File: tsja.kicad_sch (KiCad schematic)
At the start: 66 parts, among them J1 QWIIC, J2 Micro_SD_Card, J3 SAO, J4 EXT, J6 USB-C, M1 Vibration, Q1 AP2302B, Q4 AO3400 (A09T), Q5 AO3400 (A09T), T1 Select, T2 Start, T3 B, T4 A, T5 Cross, U1 74LVC1G17GW,125, U10 SY6280AAC, U11 SK6805, U12 SK6805, U13 SK6805, U14 SK6805, U15 SK6805, U2 MPR121QR2, U3 ESP32-WROVER-E, U7 CH340K, U8 SK6805, U9 SY6280AAC

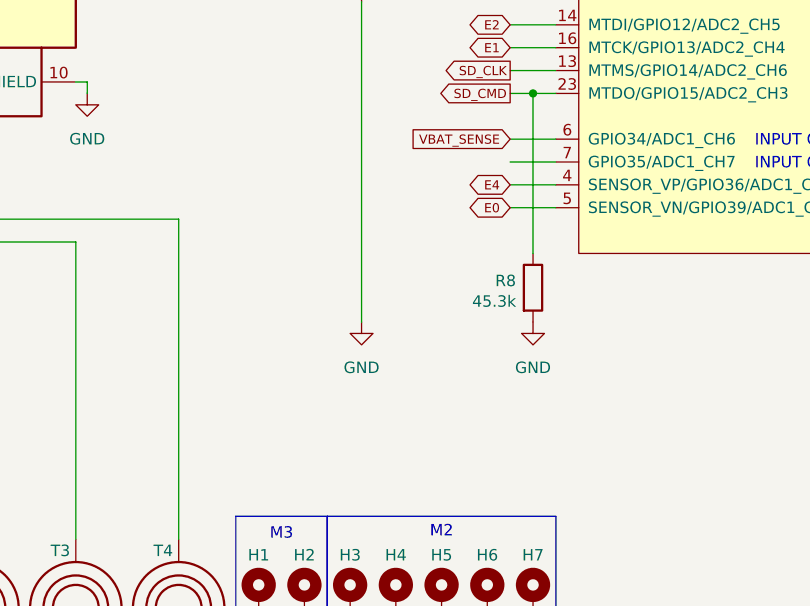
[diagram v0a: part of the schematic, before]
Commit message: Use DC/DC from WHY badge
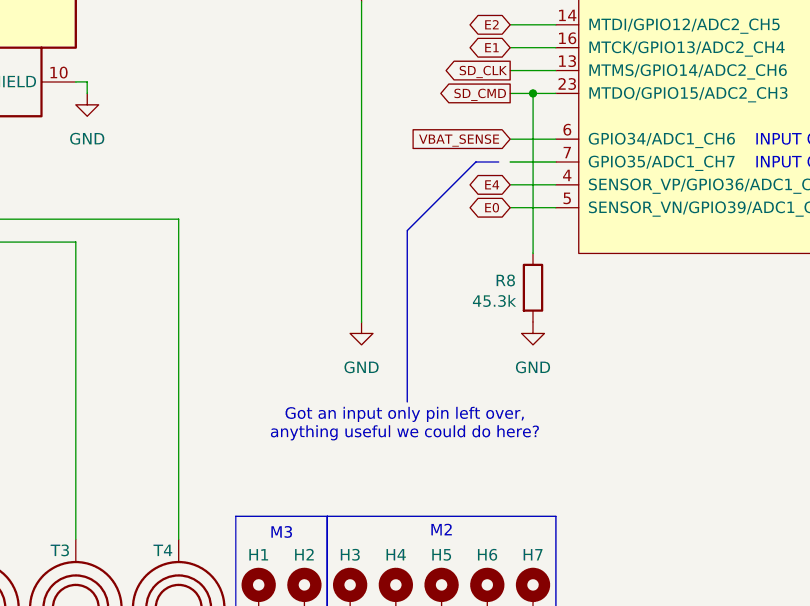
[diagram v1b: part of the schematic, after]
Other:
- note added: "Got an input only pin left over, anything useful we could do here?"
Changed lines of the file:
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@@
 	(title_block
 		(title "TSJA badge")
-		(date "2024-12-04")
+		(date "2024-12-06")
 		(rev "1.0")
 		(company "Nicolai Electronics")
@@
 		)
 	)
+	(polyline
+		(pts
+			(xy 160.02 166.37) (xy 160.02 147.32)
+		)
+		(stroke
+			(width 0)
+			(type default)
+		)
+	)
 	(wire
 		(pts
@@
 		)
 	)
+	(polyline
+		(pts
+			(xy 160.02 147.32) (xy 167.64 139.7)
+		)
+		(stroke
+			(width 0)
+			(type default)
+		)
+	)
 	(wire
 		(pts
@@
 		(pts
 			(xy 223.52 77.47) (xy 223.52 85.09)
+		)
+		(stroke
+			(width 0)
+			(type default)
+		)
+	)
+	(polyline
+		(pts
+			(xy 167.64 139.7) (xy 170.18 139.7)
 		)
 		(stroke
@@
 		)
 	)
+	(text "Got an input only pin left over,\nanything useful we could do here?"
+		(exclude_from_sim no)
+		(at 159.766 168.91 0)
+		(effects
+			(font
+				(size 1.27 1.27)
+			)
+		)
+	)

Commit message: Small fixes
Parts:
- H2: footprint MountingHole:MountingHole_3.2mm_M3_DIN965_Pad_TopOnly -> MountingHole:MountingHole_3.2mm_M3_DIN965; symbol Mechanical:MountingHole_Pad -> Mechanical:MountingHole
- H5: footprint MountingHole:MountingHole_2.7mm_M2.5_Pad_TopOnly -> MountingHole:MountingHole_2.7mm_M2.5_DIN965; symbol Mechanical:MountingHole_Pad -> Mechanical:MountingHole
- U2: LCSC (none) -> C91322
- U9: Buy early Y -> (none); Category ICs -> (none); MPN SY6280AAC -> (none); Manufacturer Silergy Corp -> (none); Mouser - -> (none); Sponsored N -> (none)
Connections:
- net GND: no longer H2.1, H5.1
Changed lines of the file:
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@@
 			)
 		)
-		(property "Mouser" "-"
-			(at 106.68 82.55 0)
-			(effects
-				(font
-					(size 1.27 1.27)
-				)
-				(hide yes)
-			)
-		)
-		(property "Price" ""
-			(at 106.68 82.55 0)
-			(effects
-				(font
-					(size 1.27 1.27)
-				)
-				(hide yes)
-			)
-		)
-		(property "Sponsored" "N"
-			(at 106.68 82.55 0)
-			(effects
-				(font
-					(size 1.27 1.27)
-				)
-				(hide yes)
-			)
-		)
-		(property "Category" "ICs"
-			(at 106.68 82.55 0)
-			(effects
-				(font
-					(size 1.27 1.27)
-				)
-				(hide yes)
-			)
-		)
-		(property "Buy early" "Y"
-			(at 106.68 82.55 0)
-			(effects
-				(font
-					(size 1.27 1.27)
-				)
-				(hide yes)
-			)
-		)
-		(property "MPN" "SY6280AAC"
-			(at 106.68 82.55 0)
-			(effects
-				(font
-					(size 1.27 1.27)
-				)
-				(hide yes)
-			)
-		)
-		(property "Manufacturer" "Silergy Corp"
-			(at 106.68 82.55 0)
-			(effects
-				(font
-					(size 1.27 1.27)
-				)
-				(hide yes)
-			)
-		)
 		(pin "1"
 		)
@@
 	)
 	(symbol
-		(lib_id "power:GND")
-		(at 148.59 190.5 0)
-		(unit 1)
-		(exclude_from_sim no)
-		(in_bom yes)
-		(on_board yes)
-		(dnp no)
-		(fields_autoplaced yes)
-		(property "Reference" "#PWR02"
-			(at 148.59 196.85 0)
-			(effects
-				(font
-					(size 1.27 1.27)
-				)
-				(hide yes)
-			)
-		)
-		(property "Value" "GND"
-			(at 148.59 195.58 0)
-			(effects
-				(font
-					(size 1.27 1.27)
-				)
-			)
-		)
-		(property "Footprint" ""
-			(at 148.59 190.5 0)
-			(effects
-				(font
-					(size 1.27 1.27)
-				)
-				(hide yes)
-			)
-		)
-		(property "Datasheet" ""
-			(at 148.59 190.5 0)
-			(effects
-				(font
-					(size 1.27 1.27)
-				)
-				(hide yes)
-			)
-		)
-		(property "Description" "Power symbol creates a global label with name \"GND\" , ground"
-			(at 148.59 190.5 0)
-			(effects
-				(font
-					(size 1.27 1.27)
-				)
-				(hide yes)
-			)
-		)
-		(pin "1"
-		)
-		(instances
-			(project "tsja"
-				(path "/5f312b85-6822-40a3-b417-2df49696ca2d"
-					(reference "#PWR02")
-					(unit 1)
-				)
-			)
-		)
-	)
-	(symbol
 		(lib_id "mch2021-rescue:C-Device")
 		(at 144.78 34.29 0)
@@
 	)
 	(symbol
-		(lib_id "power:GND")
-		(at 163.83 190.5 0)
-		(unit 1)
-		(exclude_from_sim no)
-		(in_bom yes)
-		(on_board yes)
-		(dnp no)
-		(fields_autoplaced yes)
-		(property "Reference" "#PWR020"
-			(at 163.83 196.85 0)
-			(effects
-				(font
-					(size 1.27 1.27)
-				)
-				(hide yes)
-			)
-		)
-		(property "Value" "GND"
-			(at 163.83 195.58 0)
-			(effects
-				(font
-					(size 1.27 1.27)
-				)
-			)
-		)
-		(property "Footprint" ""
-			(at 163.83 190.5 0)
-			(effects
-				(font
-					(size 1.27 1.27)
-				)
-				(hide yes)
-			)
-		)
-		(property "Datasheet" ""
-			(at 163.83 190.5 0)
-			(effects
-				(font
-					(size 1.27 1.27)
-				)
-				(hide yes)
-			)
-		)
-		(property "Description" "Power symbol creates a global label with name \"GND\" , ground"
-			(at 163.83 190.5 0)
-			(effects
-				(font
-					(size 1.27 1.27)
-				)
-				(hide yes)
-			)
-		)
-		(pin "1"
-		)
-		(instances
-			(project "tsja"
-				(path "/5f312b85-6822-40a3-b417-2df49696ca2d"
-					(reference "#PWR020")
-					(unit 1)
-				)
-			)
-		)
-	)
-	(symbol
 		(lib_id "Sensor_Touch:MPR121QR2")
 		(at 45.72 161.29 0)
@@
 			)
 		)
+		(property "LCSC" "C91322"
+			(at 45.72 161.29 0)
+			(effects
+				(font
+					(size 1.27 1.27)
+				)
+				(hide yes)
+			)
+		)
 		(pin "16"
 		)
@@
 	)
 	(symbol
-		(lib_id "Mechanical:MountingHole_Pad")
-		(at 163.83 187.96 0)
+		(lib_id "Mechanical:MountingHole")
+		(at 163.83 186.69 0)
 		(unit 1)
 		(exclude_from_sim yes)
@@
 		)
 		(property "Value" "~"
-			(at 166.37 187.9599 0)
+			(at 166.37 186.6899 0)
 			(effects
 				(font
@@
 			)
 		)
-		(property "Footprint" "MountingHole:MountingHole_2.7mm_M2.5_Pad_TopOnly"
-			(at 163.83 187.96 0)
+		(property "Footprint" "MountingHole:MountingHole_2.7mm_M2.5_DIN965"
+			(at 163.83 186.69 0)
 			(effects
 				(font
@@
 		)
 		(property "Datasheet" "~"
-			(at 163.83 187.96 0)
+			(at 163.83 186.69 0)
 			(effects
 				(font
@@
 			)
 		)
-		(property "Description" "Mounting Hole with connection"
-			(at 163.83 187.96 0)
+		(property "Description" "Mounting Hole without connection"
+			(at 163.83 186.69 0)
 			(effects
 				(font
@@
 			)
 		)
-		(pin "1"
-		)
 		(instances
 			(project "tsja"
@@
 	)
 	(symbol
-		(lib_id "Mechanical:MountingHole_Pad")
-		(at 148.59 187.96 0)
+		(lib_id "Mechanical:MountingHole")
+		(at 148.59 186.69 0)
 		(unit 1)
 		(exclude_from_sim yes)
@@
 		)
 		(property "Value" "~"
-			(at 151.13 187.9599 0)
+			(at 151.13 186.6899 0)
 			(effects
 				(font
@@
 			)
 		)
-		(property "Footprint" "MountingHole:MountingHole_3.2mm_M3_DIN965_Pad_TopOnly"
-			(at 148.59 187.96 0)
+		(property "Footprint" "MountingHole:MountingHole_3.2mm_M3_DIN965"
+			(at 148.59 186.69 0)
 			(effects
 				(font
@@
 		)
 		(property "Datasheet" "~"
-			(at 148.59 187.96 0)
+			(at 148.59 186.69 0)
 			(effects
 				(font
@@
 			)
 		)
-		(property "Description" "Mounting Hole with connection"
-			(at 148.59 187.96 0)
+		(property "Description" "Mounting Hole without connection"
+			(at 148.59 186.69 0)
 			(effects
 				(font
@@
 			)
 		)
-		(pin "1"
-		)
 		(instances

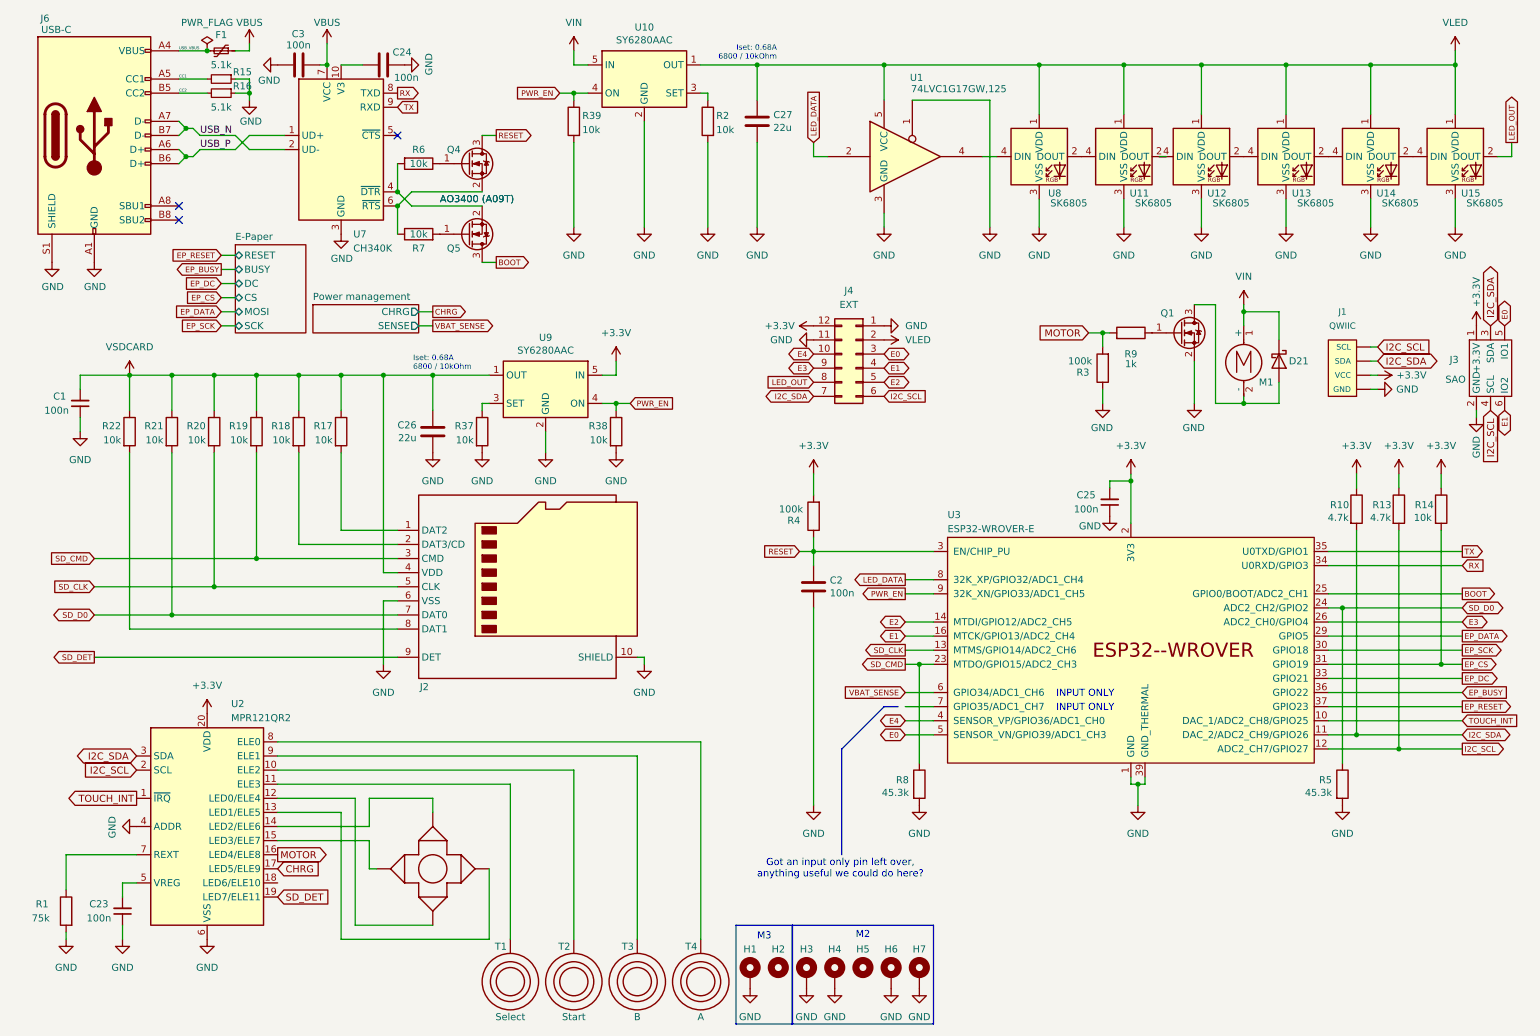
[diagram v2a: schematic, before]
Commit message: No DRC errors
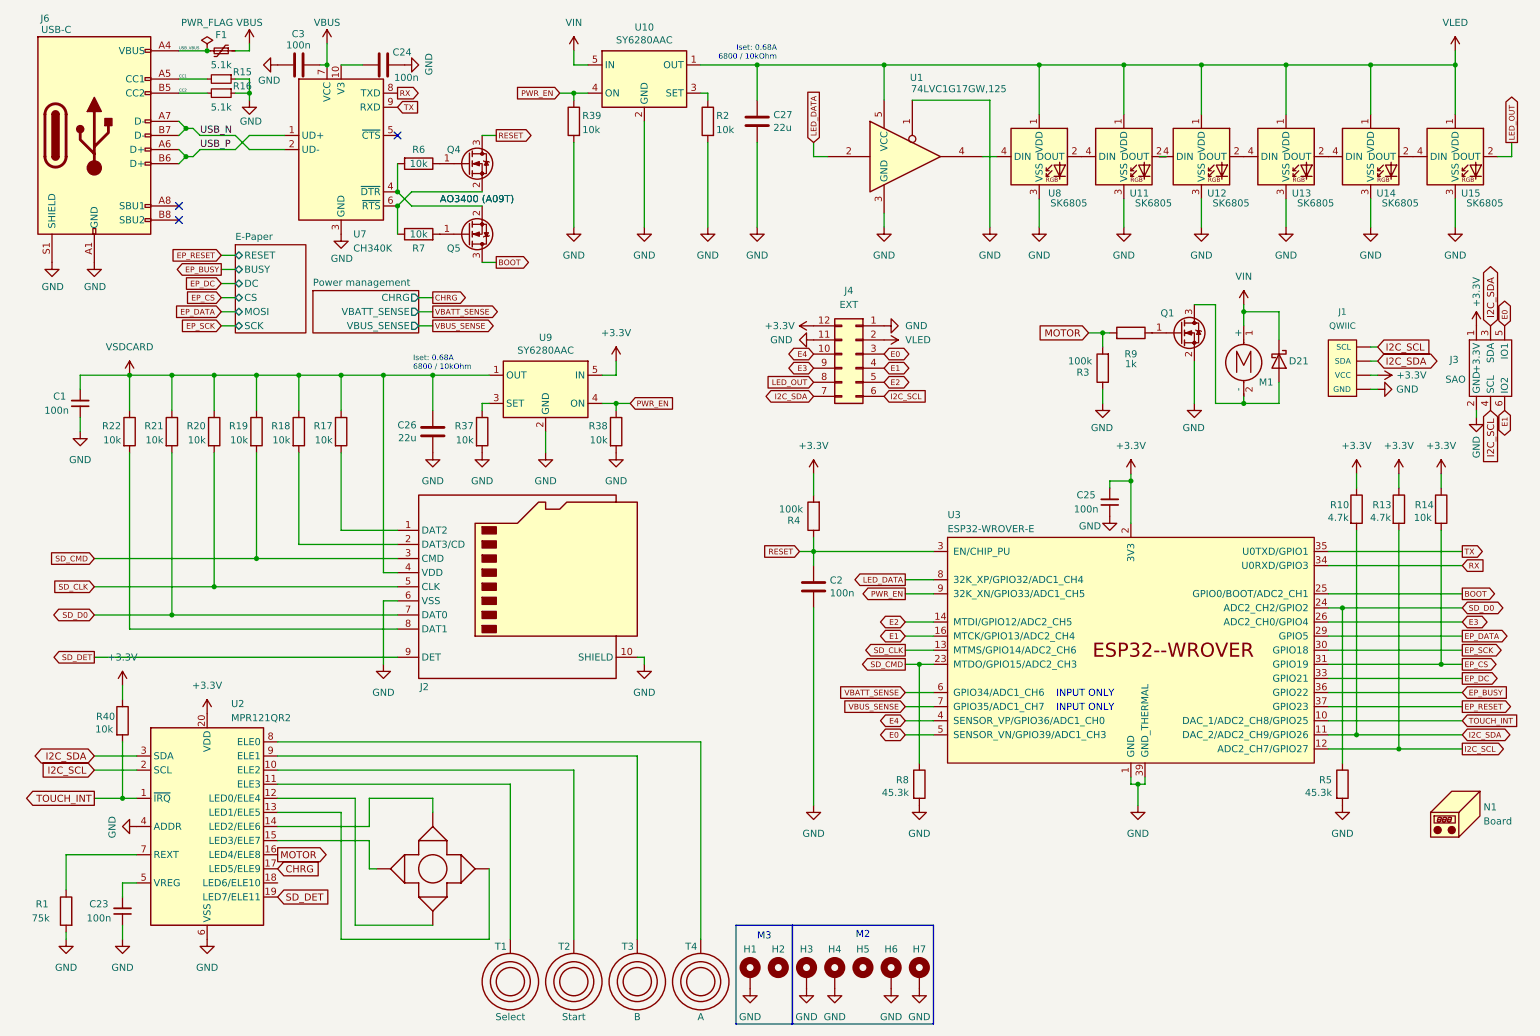
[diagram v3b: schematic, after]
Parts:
- added N1: Board, design:board, symbol Mechanical:Housing
- added R40: 10k, Resistor_SMD:R_0402_1005Metric, symbol mch2021-rescue:R-Device
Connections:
- net +3.3V: now also R40.1
- net TOUCH_INT: now also R40.2
- net VBUS_SENSE: now reaches U3.7 (GPIO35/ADC1_CH7)
- net VBAT_SENSE renamed VBATT_SENSE
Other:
- sheet Power management ports: added VBATT_SENSE, VBUS_SENSE; removed SENSE
- note removed: "Got an input only pin left over, anything useful we could do here?"

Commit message: Cleanup & tweaks
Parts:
- C2, C24, C3: LCSC C307331 -> (none)
- C26, C27: Buy early Y -> (none); Category Capacitors -> (none); LCSC C602037 -> (none); MPN CL21A226MAYNNNE -> (none); Manufacturer Samsung Electro-Mechanics -> (none); Minimal voltage rating 10 -> (none); Sponsored N -> (none); Voltage rating 25 -> (none)
- M1: footprint Connector_PinHeader_2.00mm:PinHeader_1x02_P2.00mm_Vertical -> Connector_PinHeader_2.54mm:PinHeader_1x02_P2.54mm_Vertical_SMD_Pin1Left
- R6, R7: LCSC C60490 -> (none)
- U10: Buy early Y -> (none); Category ICs -> (none); MPN SY6280AAC -> (none); Manufacturer Silergy Corp -> (none); Mouser - -> (none); Sponsored N -> (none)

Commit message: Apply fixes proposed by Paul
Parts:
- added C31: 22u, Capacitor_SMD:C_0805_2012Metric, symbol Device:C
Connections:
- net VIN: now also C31.1
- net at D21.2 (A), M1.2 (-), Q1.3 (D): now also C31.2
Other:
- moved on the sheet: D21, M1, Q1, R3, R40, R9

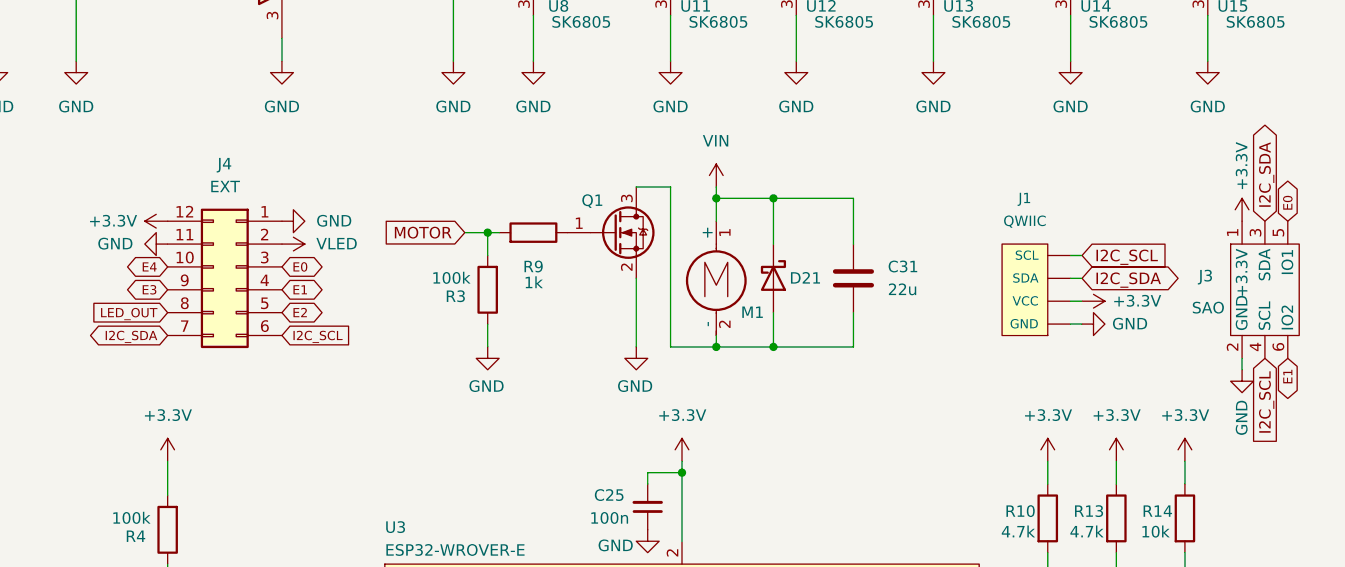
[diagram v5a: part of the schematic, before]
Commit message: Fill out BOM, add labels to PCB
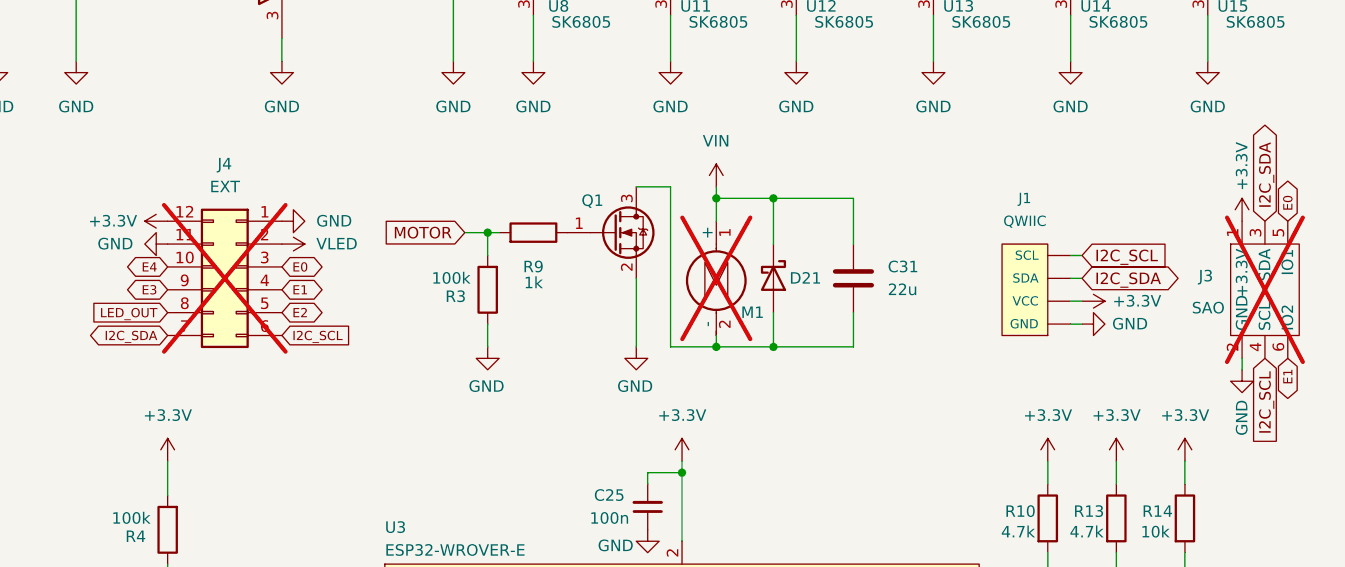
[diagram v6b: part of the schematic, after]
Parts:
- C1, C2, C23, C24, C25, C3: LCSC (none) -> C307331
- C26, C27, C31: LCSC (none) -> C45783
- H1, H2, H3, H4, H5, H6, H7: LCSC (none) -> -
- J3, J4: now not fitted; now left out of the parts list
- M1: LCSC (none) -> -; now not fitted; now left out of the parts list
- N1, T1, T2, T3, T4, T5: LCSC (none) -> -; now left out of the parts list
- R1: LCSC (none) -> C25798
- R10, R13: LCSC (none) -> C25940
- R14, R17, R18, R19, R2, R20, R21, R22, R37, R38, R39, R40, R6, R7: LCSC (none) -> C25744
- R15, R16: LCSC (none) -> C25905
- R3, R4: LCSC (none) -> C25741
- R9: LCSC (none) -> C11702
- U3: LCSC (none) -> C529589
